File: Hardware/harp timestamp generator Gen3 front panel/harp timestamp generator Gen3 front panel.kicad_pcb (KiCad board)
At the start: 2 copper layers, 133 x 35 mm, 12 parts

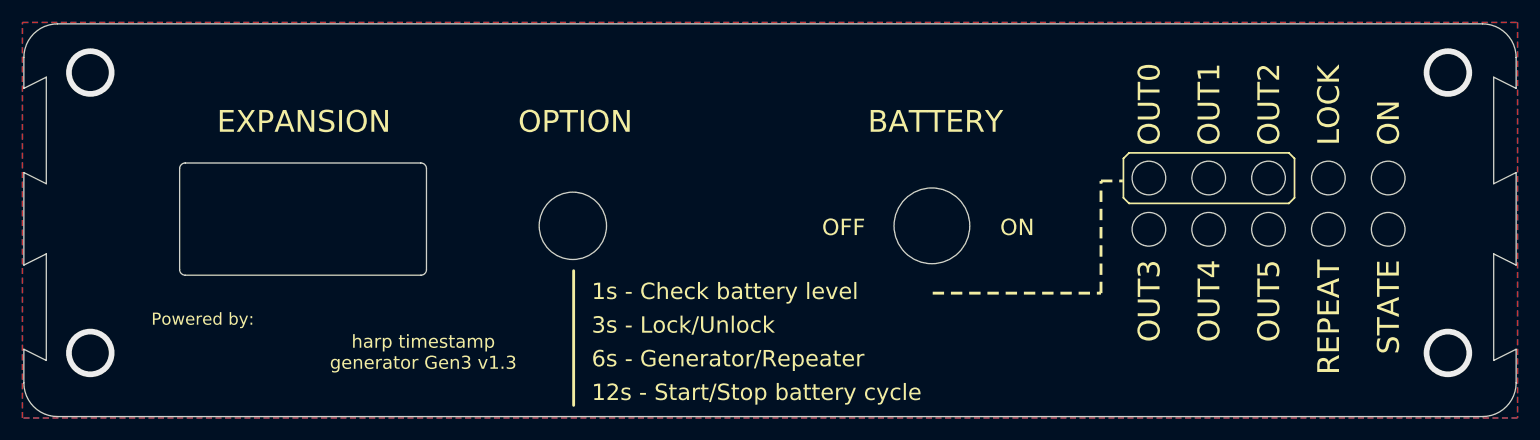
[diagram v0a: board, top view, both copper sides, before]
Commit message: review após 1ª produção de placas teste
> harp timestamp generator Gen3
  . mudança da case de Q2
  . mudança de ligação em 'Button0'

> harp timestamp generator Gen3 front panel
  . acerto no recorte da ficha IDC e interruptor bateria
  . modificação de setup no logo 'harp'

> harp timestamp generator Gen3 rear panel
  . acerto no recorte de ficha USB
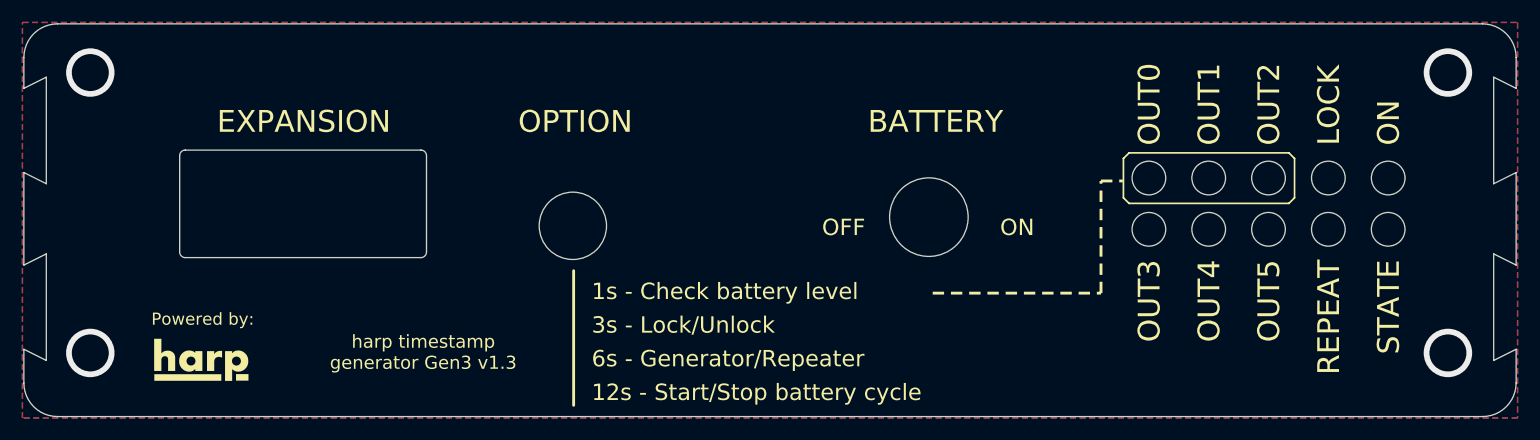
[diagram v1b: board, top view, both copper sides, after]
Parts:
- added REF**: Fiducial_Cross_1.5mm_Mask2mm, Fiducial:Fiducial_Cross_1.5mm_Mask2mm, F.Cu at (144.2, 109.1)
- moved UNK_HOLE_11 0.82 mm to (162.7, 104.7)
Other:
- outline, holes or cut-outs redrawn
